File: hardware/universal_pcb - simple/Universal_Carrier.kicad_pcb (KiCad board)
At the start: 2 copper layers, 100 x 85 mm, 24 parts, among them J1 ESP32_T_LANDSCAPE, J10 RACK_CREMALHEIRA, J11 PWR_ESP_5V, J12 PWR_SERVO_5V, J2 ESP32_B_LANDSCAPE, J3 SX1278_LORA_2x4, J4 BATT_APM, J5 BUZZER, J6 GPS_LC29H_7PIN, J7 ESC_PROP_UP, J8 RUDDER_DN, J9 WINCH_MODE, SW1 UP, SW2 MODE, SW3 DOWN, SW4 BOOT

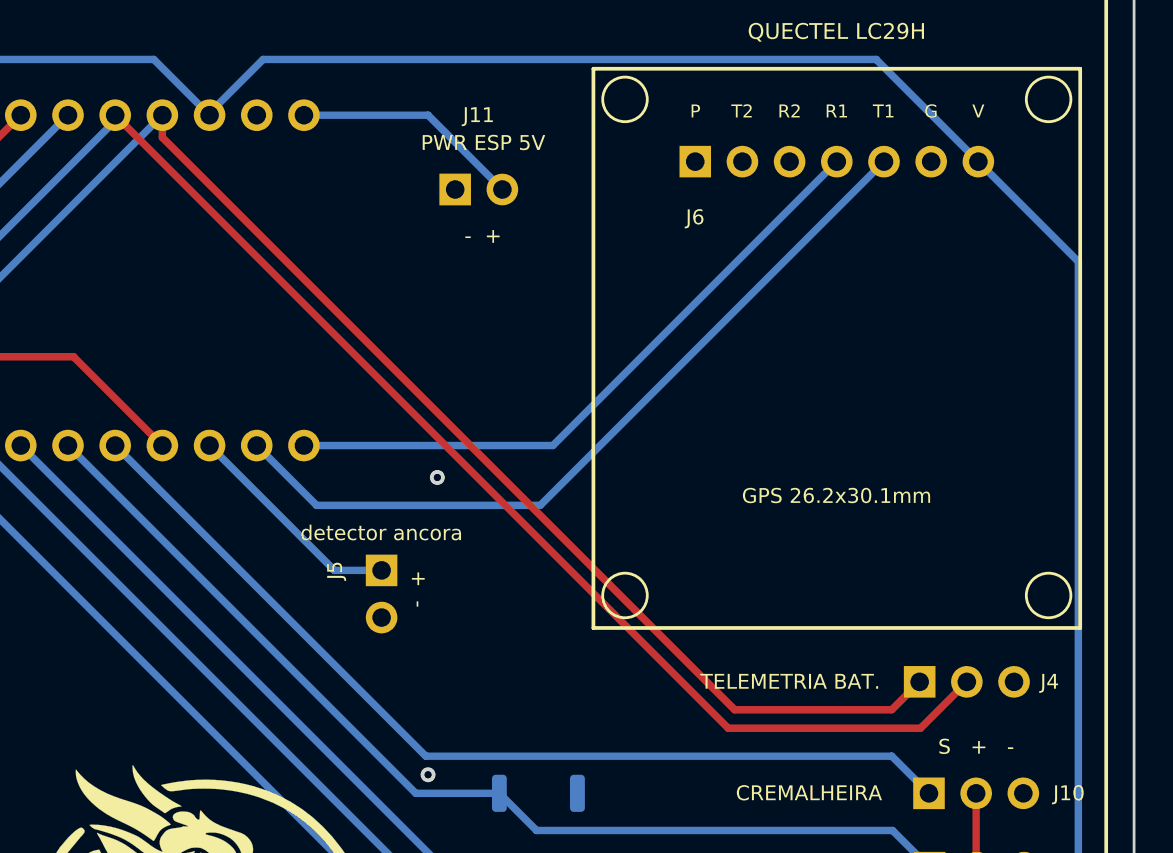
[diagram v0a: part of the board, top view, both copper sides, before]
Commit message: feat: update Universal Carrier PCB design and gerber files with I2C cleanup
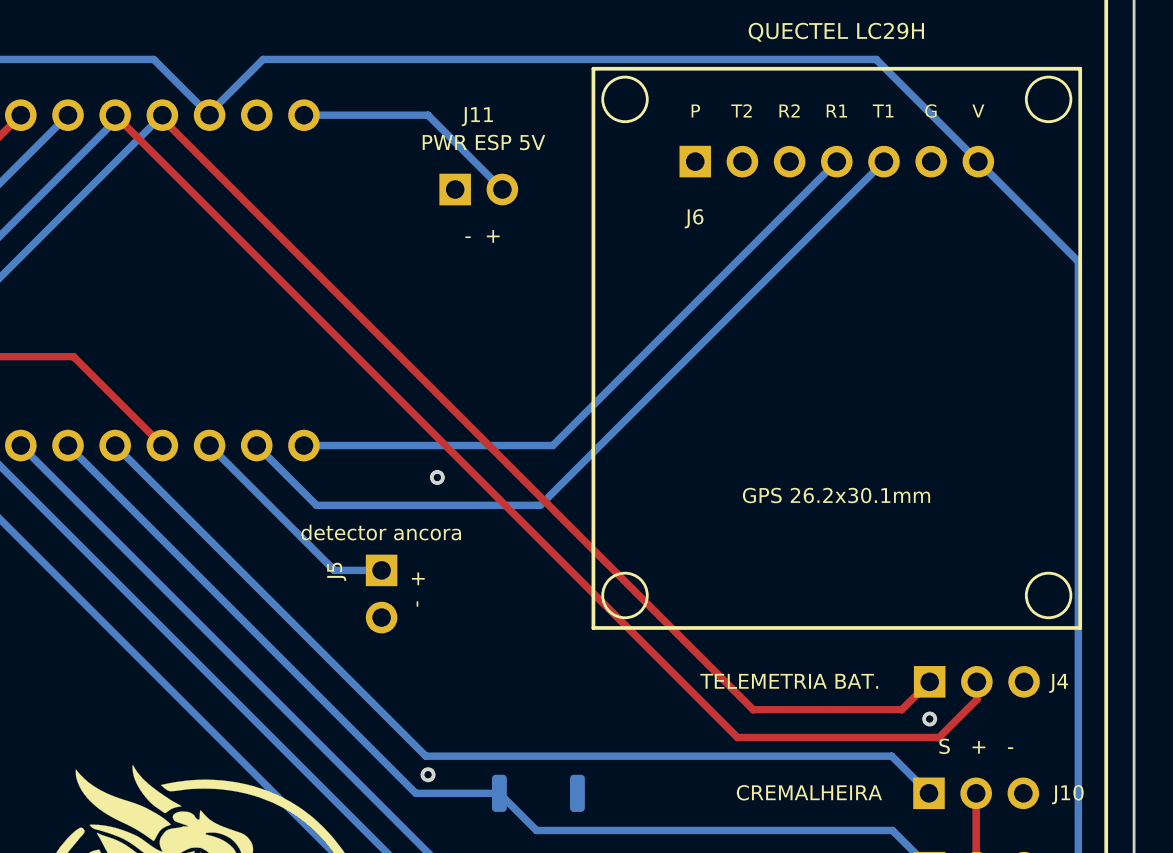
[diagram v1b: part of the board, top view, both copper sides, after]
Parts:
- moved J4 0.54 mm to (89.0, 46.5)
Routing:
- net /IO1_ADC: track 103.6 -> 105.1 mm
- net /GND: vias 6 -> 7
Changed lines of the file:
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@@
 	(footprint "Connector_PinHeader_2.54mm:PinHeader_1x03_P2.54mm_Horizontal"
 		(layer "F.Cu")
-		(at 88.46 46.5)
+		(at 89 46.5)
 		(property "Reference" "J4"
 			(at 7 0 0)
@@
 	)
 	(via
+		(at 89 48.5)
+		(size 0.8)
+		(drill 0.4)
+		(layers "F.Cu" "B.Cu")
+		(free yes)
+		(net "/GND")
+	)
+	(via
 		(at 22 14)
 		(size 0.8)
@@
 	)
 	(segment
-		(start 86.96 48)
-		(end 78.5 48)
+		(start 88.46 47.04)
+		(end 87.5 48)
 		(width 0.4)
 		(layer "F.Cu")
@@
 	)
 	(segment
-		(start 78.5 48)
-		(end 47.7 17.2)
+		(start 87.5 48)
+		(end 79.5 48)
 		(width 0.4)
 		(layer "F.Cu")
@@
 	)
 	(segment
-		(start 47.7 17.2)
+		(start 79.5 48)
+		(end 47.7 16.2)
+		(width 0.4)
+		(layer "F.Cu")
+		(net "/IO0_ADC")
+	)
+	(segment
+		(start 47.7 16.2)
 		(end 47.7 16)
 		(width 0.4)
@@
 	(segment
 		(start 88.46 46.5)
-		(end 86.96 48)
+		(end 88.46 47.04)
 		(width 0.4)
 		(layer "F.Cu")
@@
 	)
 	(segment
-		(start 91 46.5)
-		(end 88.5 49)
+		(start 91.54 46.5)
+		(end 91.54 47.46)
 		(width 0.4)
 		(layer "F.Cu")
@@
 	)
 	(segment
-		(start 88.5 49)
-		(end 78.16 49)
+		(start 78.66 49.5)
+		(end 45.16 16)
 		(width 0.4)
 		(layer "F.Cu")
@@
 	)
 	(segment
-		(start 78.16 49)
-		(end 45.16 16)
+		(start 89.5 49.5)
+		(end 78.66 49.5)
+		(width 0.4)
+		(layer "F.Cu")
+		(net "/IO1_ADC")
+	)
+	(segment
+		(start 91.54 47.46)
+		(end 89.5 49.5)
 		(width 0.4)
 		(layer "F.Cu")
